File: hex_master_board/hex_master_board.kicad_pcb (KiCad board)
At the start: 2 copper layers, 105 parts, among them J1 USB_B_Micro, SW1 SW_DIP_x01, SW10 SW_DIP_x01, SW11 SW_DIP_x01, SW12 SW_DIP_x01, SW2 SW_DIP_x01, SW3 SW_DIP_x01, SW4 SW_DIP_x01, SW5 SW_DIP_x01, SW6 SW_DIP_x01, SW7 SW_DIP_x01, SW8 SW_DIP_x01, SW9 SW_DIP_x01, U1 Jack_CP-002B-ND, U10 EXB-2HV221JV, U11 EXB-2HV221JV, U12 Jack_CP-002B-ND, U13 Servo_connector, U14 Servo_connector, U15 Servo_connector, U16 Servo_connector, U17 Servo_connector, U18 Servo_connector, U19 Servo_connector, U2 74LVC1G157GV_MUX2, U20 Servo_connector, U21 Servo_connector, U22 Servo_connector, U23 Servo_connector, U24 Servo_connector, U25 Servo_connector, U26 Servo_connector, U27 Servo_connector, U28 Servo_connector, U29 EXB-2HV221JV, U3 AP2210N-5.0TRG1-lin-reg, U30 EXB-2HV221JV, U31 Servo_connector, U32 Servo_connector, U33 Servo_connector, U34 Servo_connector, U35 Servo_connector, U36 Servo_connector, U37 Servo_connector, U38 Servo_connector, U39 Servo_connector, U4 FT232RL, U40 Servo_connector, U41 Servo_connector, U42 Servo_connector, U43 Servo_connector, U44 Servo_connector, U45 Servo_connector, U46 Servo_connector, U48 header_0.1_8, U49 header_0.1_8, U5 TPS2113A, U50 header_0.1_8, U7 ATmega2561-16AU, U8 PCA9685PW, U9 PCA9685PW

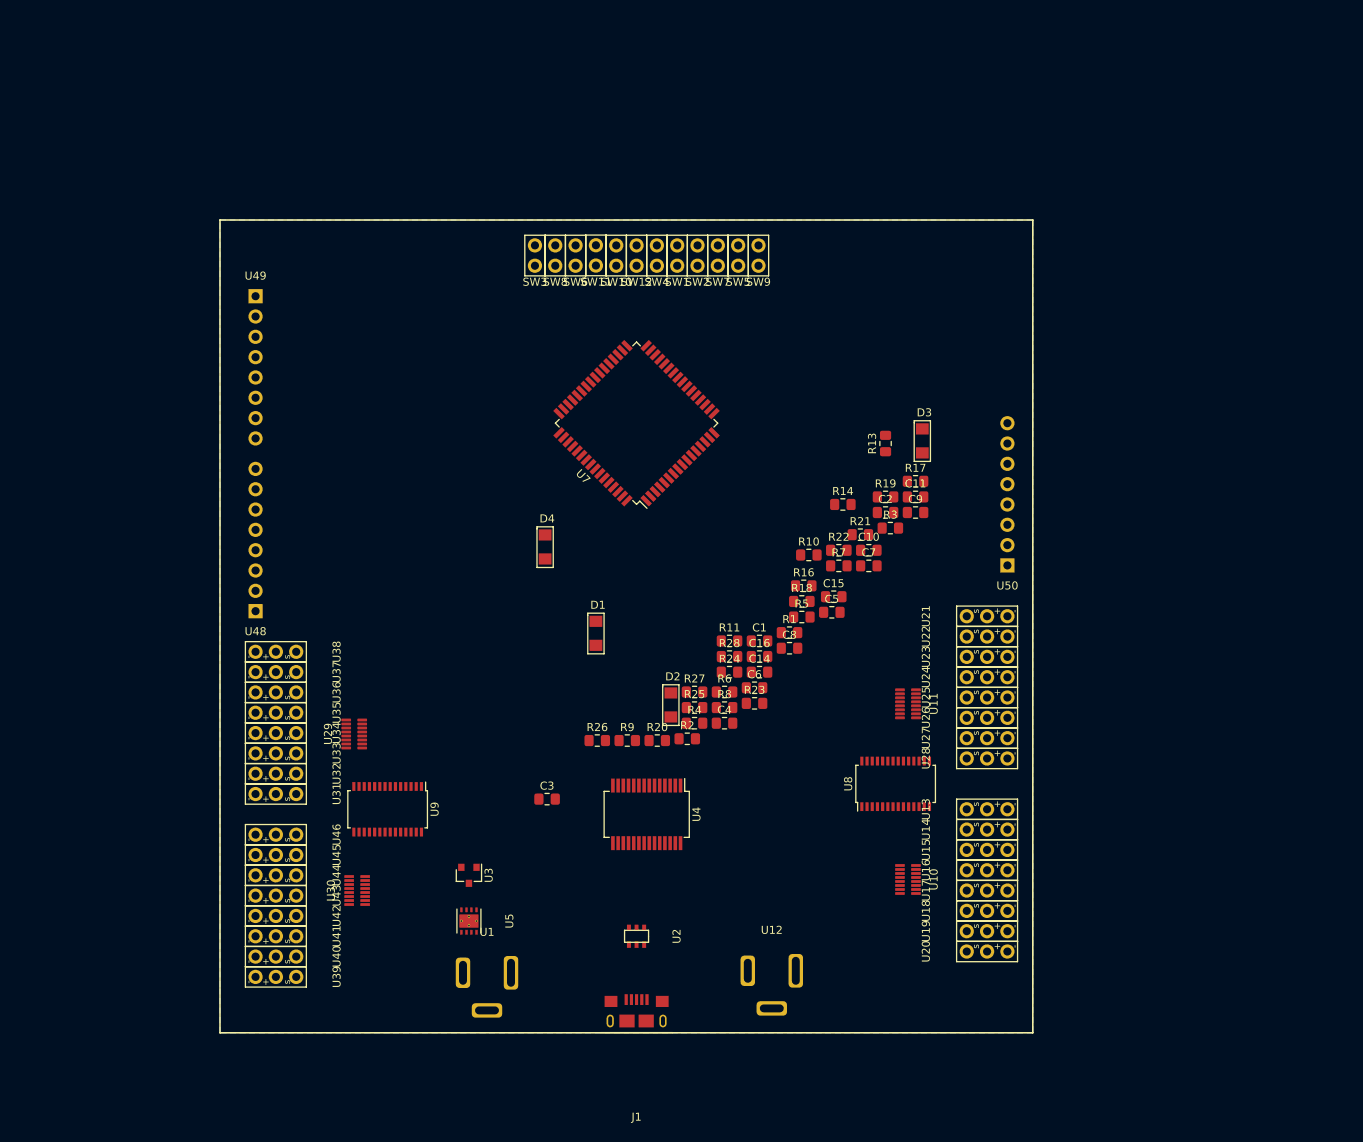
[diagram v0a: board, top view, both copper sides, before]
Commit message: Footprint for crystal, develop footprint further
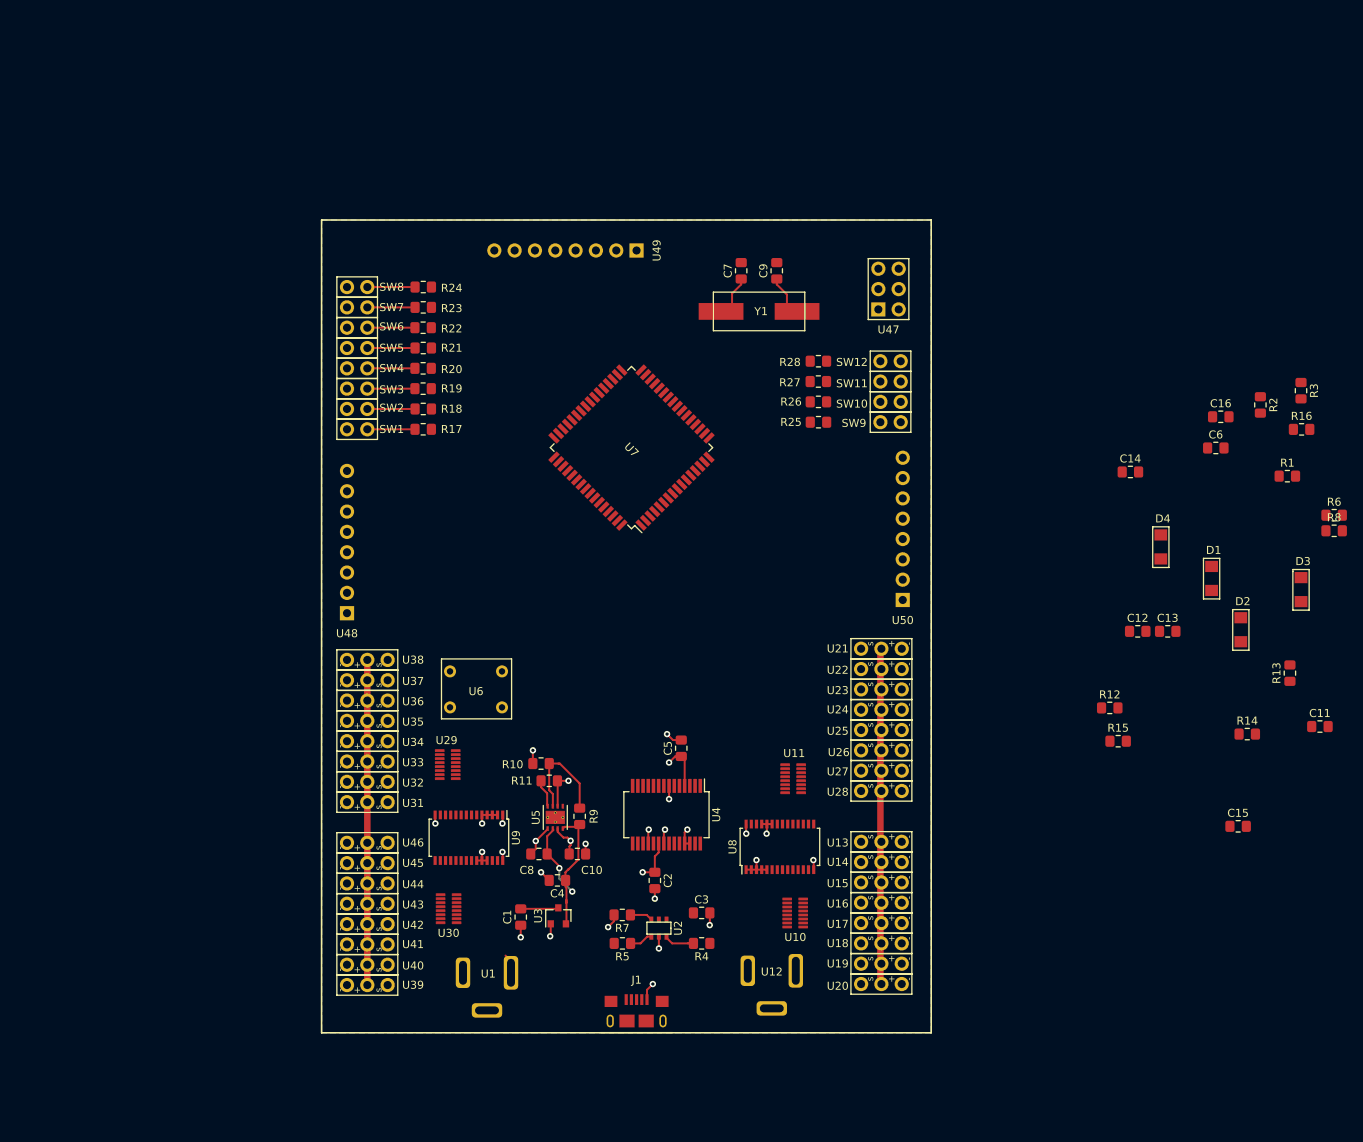
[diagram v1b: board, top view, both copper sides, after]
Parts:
- added C12: 0.1uF, Capacitor_SMD:C_0805_2012Metric_Pad1.15x1.40mm_HandSolder, F.Cu at (140.1, 76.8)
- added C13: 0.1uF, Capacitor_SMD:C_0805_2012Metric_Pad1.15x1.40mm_HandSolder, F.Cu at (143.9, 76.8)
- added R12: 1k, Resistor_SMD:R_0805_2012Metric_Pad1.15x1.40mm_HandSolder, F.Cu at (136.6, 86.4)
- added R15: 1k, Resistor_SMD:R_0805_2012Metric_Pad1.15x1.40mm_HandSolder, F.Cu at (137.7, 90.6)
- added U47: ICSP_breakout, hex_master_board:ICSP_header_0.1, F.Cu at (109.0, 36.6)
- added U6: Pushbutton_Stockroom, hex_master_board:Pushbutton_Stockroom, F.Cu at (57.4, 84.1)
- added Y1: Crystal, hex_master_board:Crystal_osc_535-10226-1-ND, F.Cu at (92.8, 34.3)
- moved R2 82.9 mm to (155.4, 48.5), turned to 270 degrees
- moved R6 79.3 mm to (164.7, 62.3)
- moved R8 79.3 mm to (164.7, 64.3)
- moved D1 77.3 mm to (149.4, 68.7)
- moved D4 77.0 mm to (143.0, 64.8)
- moved D2 71.9 mm to (153.0, 75.1)
- moved R1 65.2 mm to (158.8, 57.4)
- moved R16 65.2 mm to (160.6, 51.6)
- moved C16 65.0 mm to (150.5, 50.0)
- moved C6 65.0 mm to (149.9, 53.9)
- moved R23 64.5 mm to (50.8, 36.3), turned to 180 degrees
- moved R17 61.9 mm to (50.8, 51.6), turned to 180 degrees
- moved R24 61.5 mm to (50.8, 33.8), turned to 180 degrees
- moved R21 59.4 mm to (50.8, 41.4), turned to 180 degrees
- moved R19 59.4 mm to (50.8, 46.5), turned to 180 degrees
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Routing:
- net /servo_power: track 0.00 -> 82.8 mm
- net GND: track 0.00 -> 47.4 mm, vias 0 -> 23
- net +5V: track 0.00 -> 18.3 mm, vias 0 -> 6
- net Net-(C4-Pad1): track 0.00 -> 15.0 mm
- net Net-(R10-Pad1): track 0.00 -> 13.2 mm
- net /USB_V+: track 0.00 -> 12.2 mm, vias 0 -> 2
- net /D4: track 0.00 -> 6.02 mm
- net /D3: track 0.00 -> 5.97 mm
- net /D1: track 0.00 -> 5.97 mm
- net /D0: track 0.00 -> 5.97 mm
- net /D5: track 0.00 -> 5.89 mm
- net /D2: track 0.00 -> 5.89 mm
- net /D7: track 0.00 -> 5.84 mm
- net /D6: track 0.00 -> 5.84 mm
- net Net-(C1-Pad1): track 0.00 -> 5.06 mm
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
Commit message: More progress on layout
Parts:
- U48: value header_0.1_8 -> header_0.1_8_powered; footprint hex_master_board:header_0.1_8x -> hex_master_board:header_0.1_8_power
- moved C11 143.1 mm to (28.9, 38.4), turned to 180 degrees
- moved R13 137.1 mm to (25.4, 52.1)
- moved R6 136.1 mm to (29.0, 52.1), turned to 90 degrees
- moved D3 135.7 mm to (25.4, 57.7)
- moved R14 132.3 mm to (44.7, 14.8), turned to 270 degrees
- moved R1 126.4 mm to (32.5, 52.1), turned to 90 degrees
- moved D2 125.3 mm to (29.0, 57.7)
- moved R16 124.7 mm to (41.4, 14.8), turned to 270 degrees
- moved R15 122.0 mm to (21.8, 52.1), turned to 90 degrees
- moved D4 121.4 mm to (21.8, 57.7)
- moved R3 120.9 mm to (41.1, 65.8)
- moved C14 118.8 mm to (21.3, 71.6), turned to 180 degrees
- moved R8 118.6 mm to (47.5, 82.8), turned to 180 degrees
- moved D1 117.4 mm to (32.5, 57.7)
- moved C12 113.1 mm to (33.0, 40.6), turned to 180 degrees
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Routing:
- net +5V: track 18.3 -> 179.3 mm, vias 6 -> 24
- net /~RESET: track 0.00 -> 97.5 mm, vias 0 -> 2
- net /servo_power: track 82.8 -> 158.2 mm
- net /SCK: track 0.00 -> 45.1 mm
- net /D19: track 0.00 -> 42.4 mm, vias 0 -> 2
- net /D13: track 0.00 -> 42.1 mm
- net /D20: track 0.00 -> 42.0 mm, vias 0 -> 2
- net /A0: track 0.00 -> 40.0 mm
- net /D14: track 0.00 -> 39.2 mm
- net /A1: track 0.00 -> 37.9 mm
- net /MISO: track 0.00 -> 37.1 mm, vias 0 -> 2
- net /D15: track 0.00 -> 36.9 mm
- net /MOSI: track 0.00 -> 36.5 mm, vias 0 -> 2
- net /A2: track 0.00 -> 35.6 mm
- net /D16: track 0.00 -> 34.4 mm
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
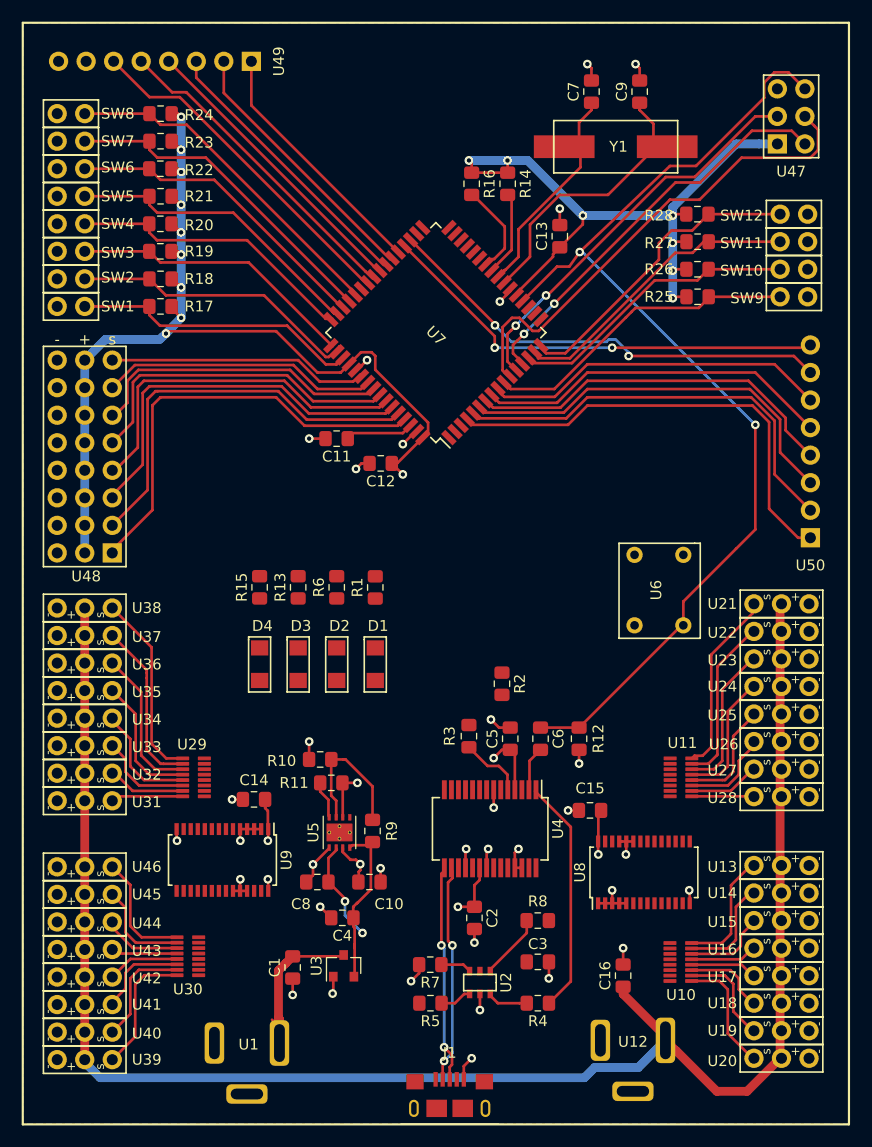
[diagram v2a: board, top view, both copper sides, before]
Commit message: Add accelerometer, more tracing
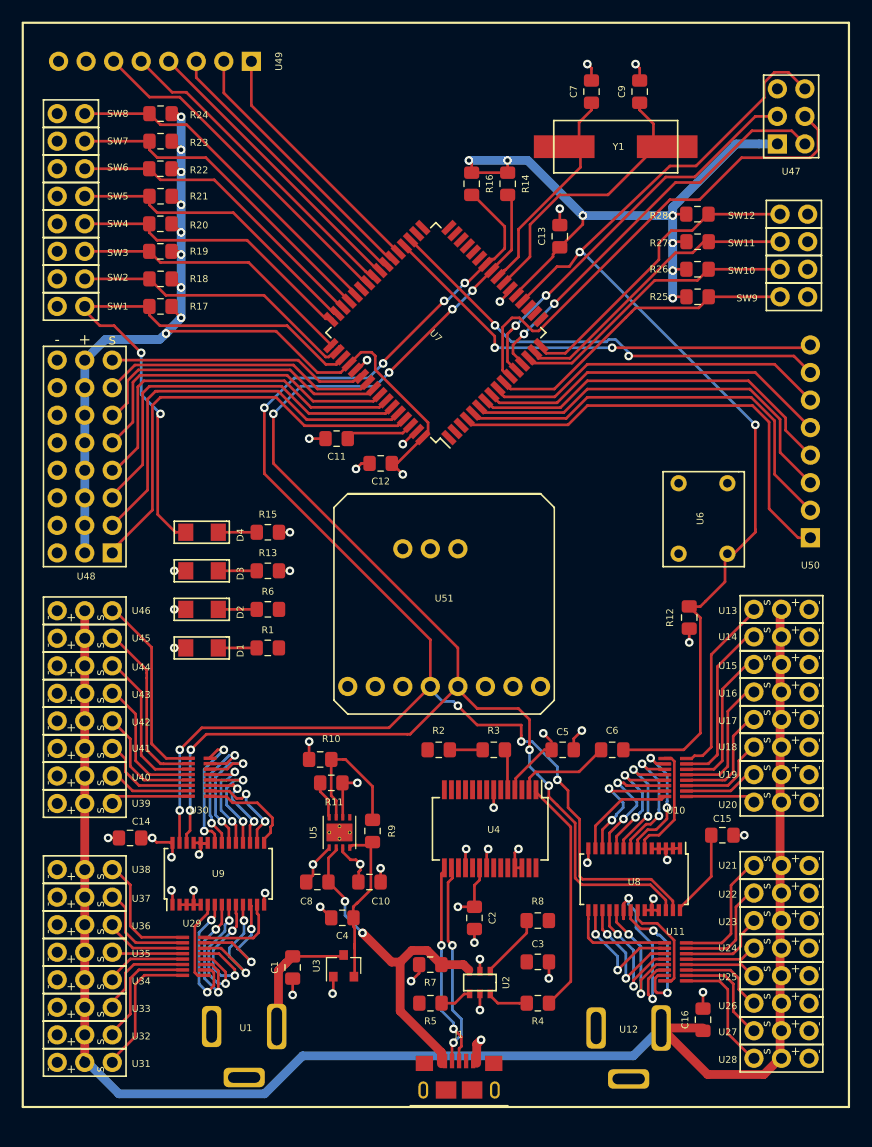
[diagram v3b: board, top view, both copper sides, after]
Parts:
- added U51: LIS3DH_breakout, hex_master_board:LIS3DH_IMU_BOARD, F.Cu at (37.6, 61.2)
- moved U26 24.1 mm to (64.9, 90.4)
- moved U28 24.1 mm to (64.9, 95.5)
- moved U31 24.1 mm to (10.8, 95.9)
- moved U33 24.1 mm to (10.8, 90.8)
- moved U21 24.1 mm to (64.9, 77.7)
- moved U23 24.1 mm to (64.9, 82.8)
- moved U25 24.1 mm to (64.9, 87.9)
- moved U36 24.1 mm to (10.8, 83.2)
- moved U38 24.1 mm to (10.8, 78.1)
- moved U22 24.1 mm to (64.9, 80.3)
- moved U24 24.1 mm to (64.9, 85.3)
- moved U27 24.1 mm to (64.9, 93.0)
- moved U32 24.1 mm to (10.8, 93.3)
- moved U34 24.1 mm to (10.8, 88.3)
- moved U35 24.1 mm to (10.8, 85.7)
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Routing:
- net /SDA: track 8.46 -> 137.8 mm, vias 0 -> 9
- net /SCL: track 7.52 -> 136.4 mm, vias 0 -> 8
- net /D0: track 27.2 -> 53.2 mm, vias 0 -> 2
- net /USB_V+: track 12.2 -> 32.6 mm
- net Net-(U11-Pad6): track 0.00 -> 17.1 mm, vias 0 -> 2
- net Net-(U29-Pad5): track 0.00 -> 13.0 mm, vias 0 -> 2
- net Net-(U11-Pad7): track 0.00 -> 12.8 mm, vias 0 -> 2
- net Net-(U29-Pad3): track 0.00 -> 12.7 mm, vias 0 -> 2
- net Net-(U11-Pad5): track 0.00 -> 12.7 mm, vias 0 -> 2
- net Net-(U30-Pad6): track 0.00 -> 12.6 mm, vias 0 -> 2
- net Net-(U10-Pad6): track 0.00 -> 12.5 mm, vias 0 -> 2
- net Net-(U29-Pad4): track 0.00 -> 12.4 mm, vias 0 -> 2
- net Net-(U10-Pad5): track 0.00 -> 12.2 mm, vias 0 -> 2
- net Net-(U11-Pad4): track 0.00 -> 12.2 mm, vias 0 -> 2
- net Net-(U30-Pad7): track 0.00 -> 12.1 mm, vias 0 -> 2
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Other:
- net class Default: clearance 0.2 -> 0.1524
- rule trace_clearance: 0.2 -> 0.1524
- rule trace_min: 0.2 -> 0.1778

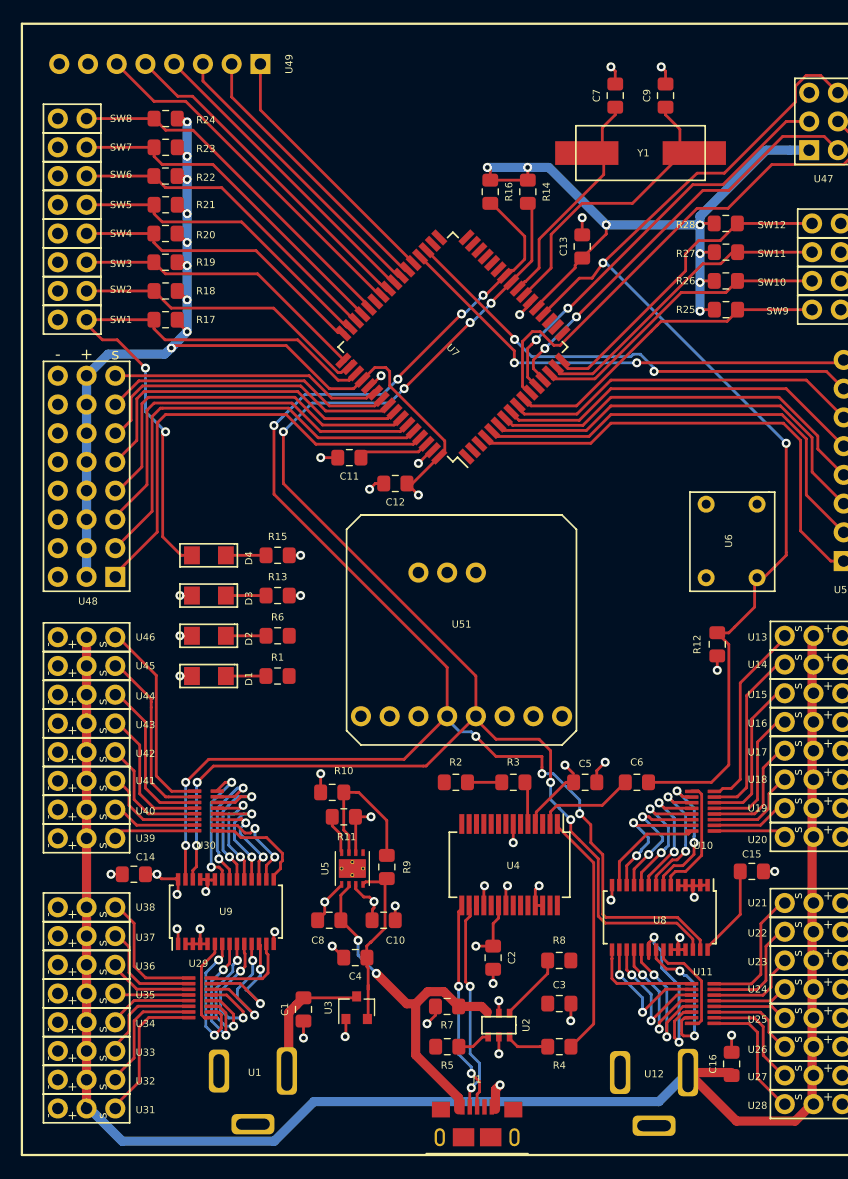
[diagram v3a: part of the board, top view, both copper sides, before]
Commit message: Add I2C headers, fully connect board
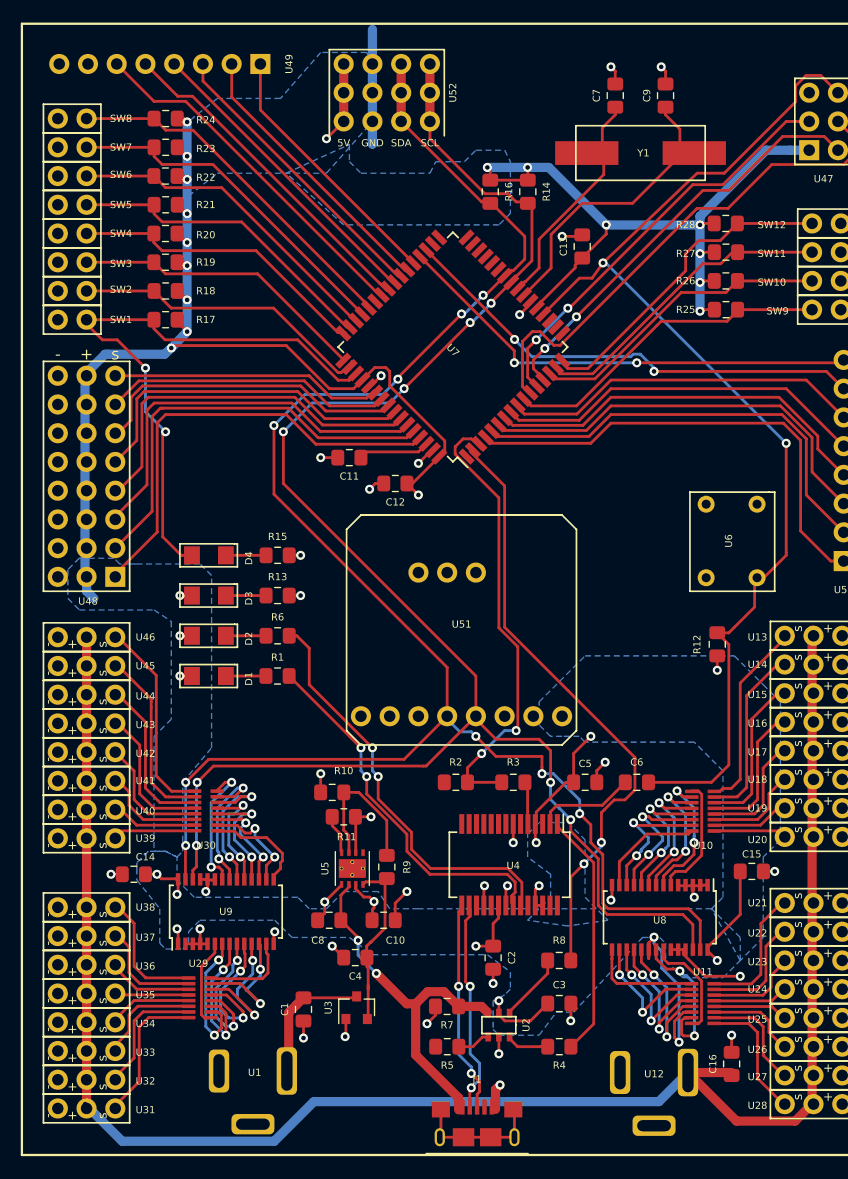
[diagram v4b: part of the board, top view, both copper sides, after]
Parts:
- added U52: header_0.1_I2C, hex_master_board:header_0.1_i2c_12, F.Cu at (32.3, 2.29)
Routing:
- net /Atmega_RXD0: track 0.00 -> 53.9 mm, vias 0 -> 2
- net /Atmega_TXD0: track 3.28 -> 40.7 mm, vias 0 -> 2
- net /~RX_LED: track 0.00 -> 37.1 mm, vias 0 -> 2
- net /~TX_LED: track 0.00 -> 32.5 mm, vias 0 -> 2
- net +5V: track 189.3 -> 210.9 mm, vias 28 -> 31
- net /SCL: track 136.4 -> 154.1 mm
- net GND: track 66.1 -> 83.1 mm
- net /SDA: track 137.8 -> 153.9 mm
- net Net-(J1-Pad6): track 0.00 -> 11.4 mm
- added copper zone on B.Cu, net +5V
